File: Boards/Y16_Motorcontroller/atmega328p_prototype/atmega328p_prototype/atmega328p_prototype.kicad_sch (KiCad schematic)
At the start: 14 parts, among them J1 Conn_02x03_Odd_Even, U1 ATMEGA328P-AU, U2 CH340G, Y1 Crystal

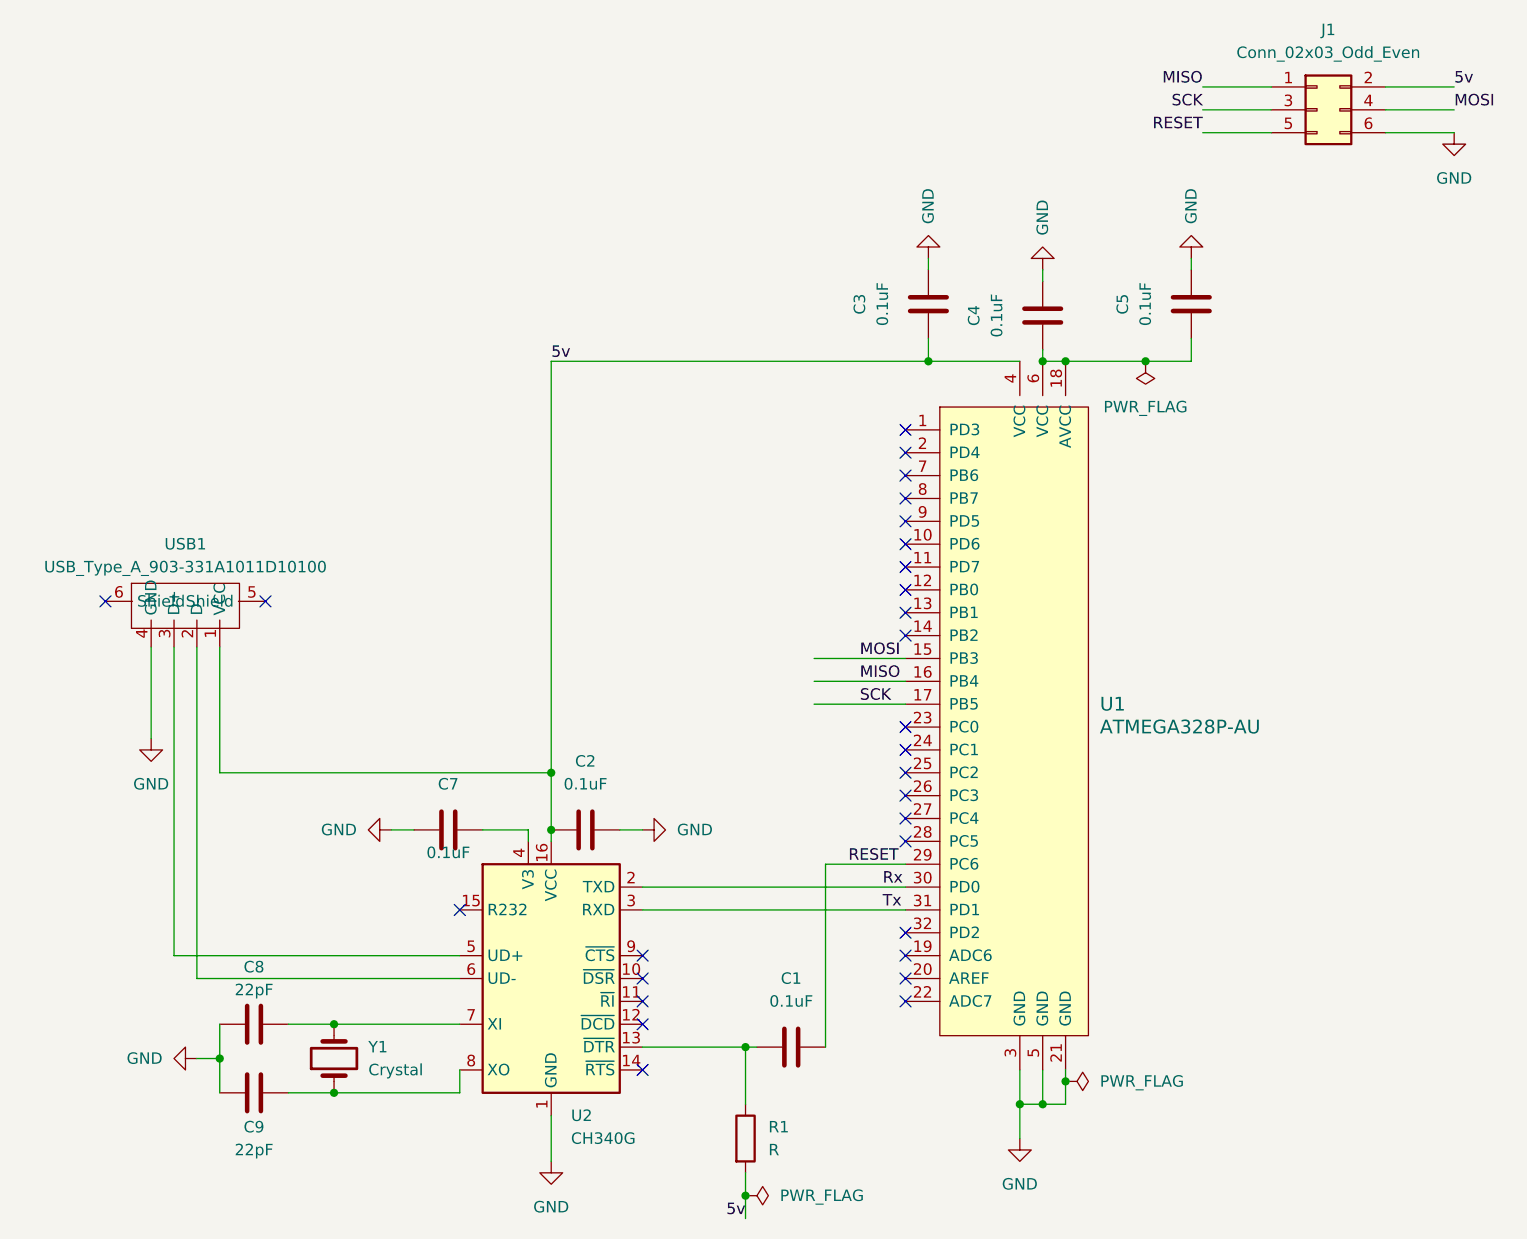
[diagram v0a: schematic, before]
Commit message: added Y16_motorControllerConversion project files
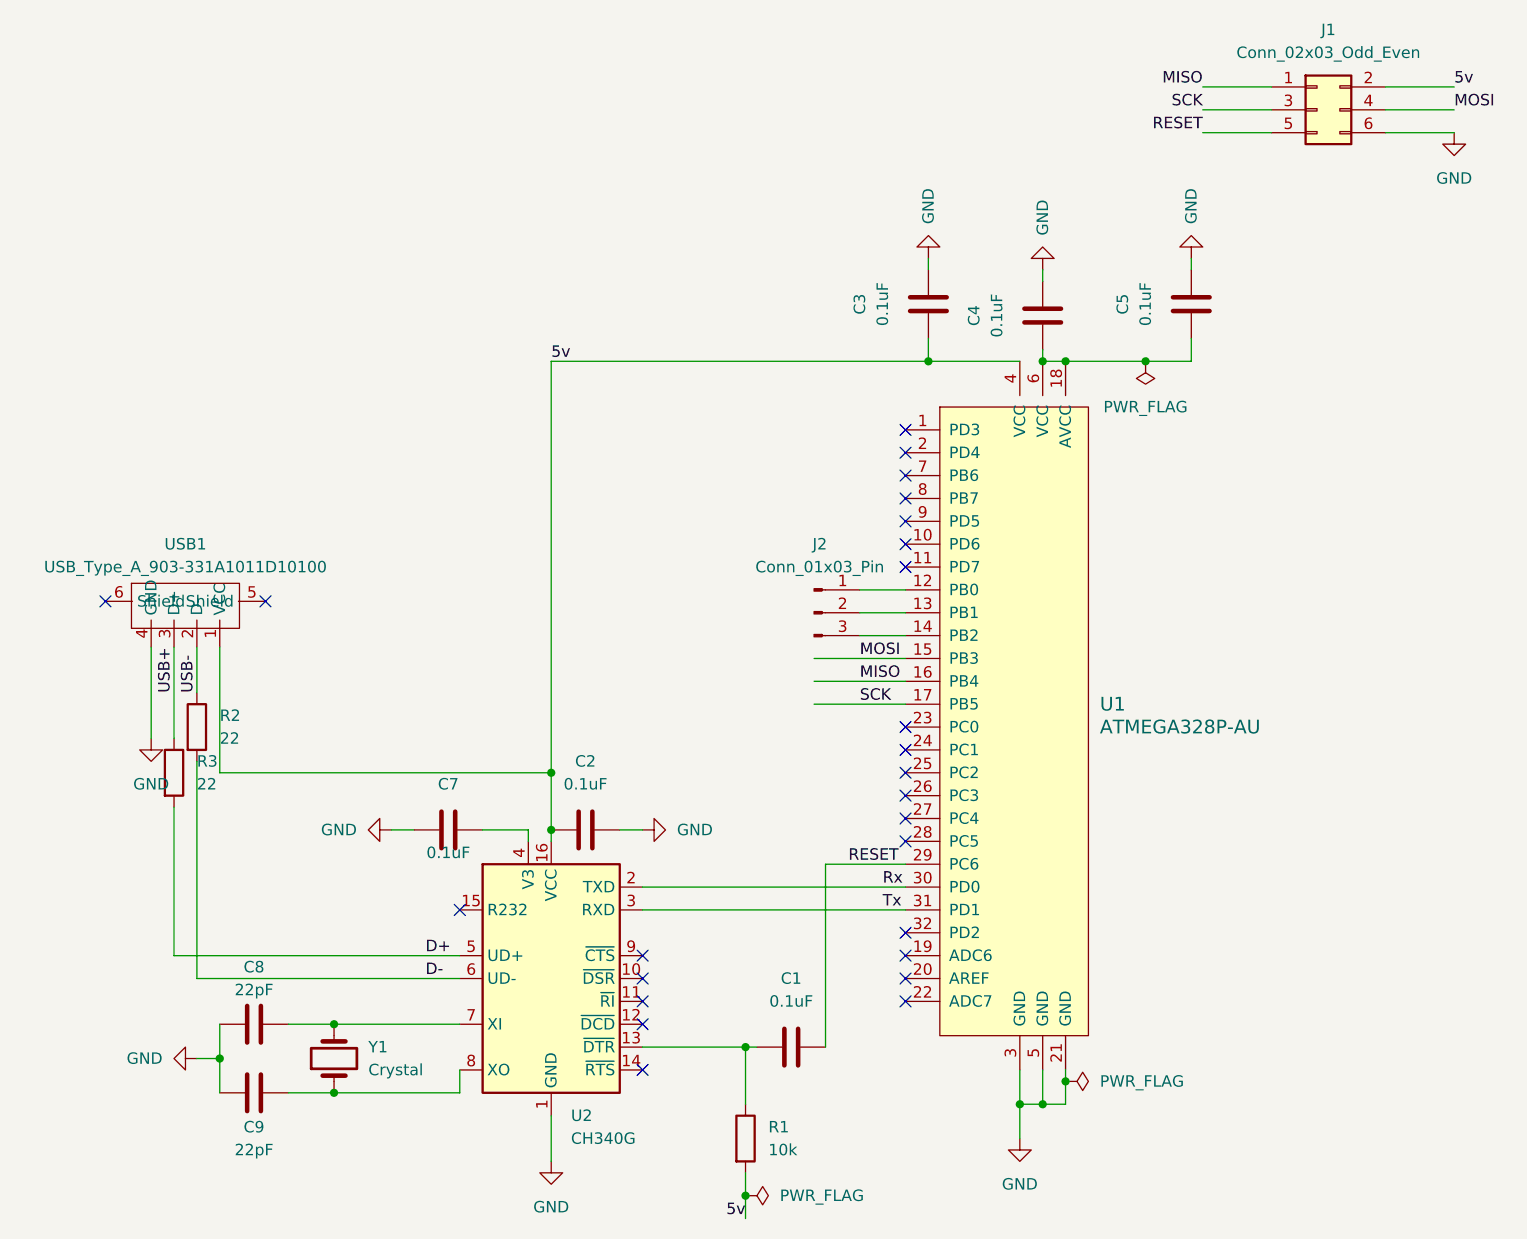
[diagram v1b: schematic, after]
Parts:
- added J2: Conn_01x03_Pin, Connector_PinHeader_2.54mm:PinHeader_1x03_P2.54mm_Vertical, symbol Connector:Conn_01x03_Pin
- added R2, R3: 22, Resistor_SMD:R_0603_1608Metric, symbol Device:R
- C1, C2, C3, C4, C5, C7, C8, C9: footprint (none) -> Capacitor_SMD:C_0603_1608Metric
- J1: footprint (none) -> Connector_PinHeader_2.54mm:PinHeader_2x03_P2.54mm_Vertical
- R1: value R -> 10k; footprint (none) -> Resistor_SMD:R_0603_1608Metric
- USB1: footprint (none) -> PiE_Footprints:USB-A_female
- Y1: footprint (none) -> PiE_Footprints:JYJE S1C12000VWFAC
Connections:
- net at U1.12 (PB0): now also J2.1 (Pin_1)
- net at U1.13 (PB1): now also J2.2 (Pin_2)
- net at U1.14 (PB2): now also J2.3 (Pin_3)
- net D+: now reaches U2.5 (UD+)
- net D+: now also R3.2; no longer USB1.3 (D+)
- net D-: now reaches U2.6 (UD-)
- net D-: now also R2.2; no longer USB1.2 (D-)
- new net USB+: R3.1, USB1.3 (D+)
- new net USB-: R2.1, USB1.2 (D-)
- no-connect marks 28 -> 25
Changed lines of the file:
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@@
   (no_connect (at 116.84 114.3))
   (no_connect (at 166.37 121.92))
-  (no_connect (at 166.37 66.04))
   (no_connect (at 166.37 106.68))
   (no_connect (at 166.37 76.2))
   (no_connect (at 166.37 96.52))
-  (no_connect (at 166.37 63.5))
   (no_connect (at 137.16 127))
   (no_connect (at 137.16 121.92))
-  (no_connect (at 166.37 83.82))
   (no_connect (at 137.16 119.38))
+  (no_connect (at 166.37 60.96))
   (no_connect (at 166.37 93.98))
   (no_connect (at 166.37 101.6))
@@
   (no_connect (at 166.37 104.14))
   (no_connect (at 166.37 99.06))
-  (no_connect (at 166.37 81.28))
   (no_connect (at 166.37 119.38))
   (no_connect (at 95.25 80.01))
   (no_connect (at 137.16 132.08))
-  (no_connect (at 166.37 60.96))
   (no_connect (at 166.37 116.84))
   (no_connect (at 77.47 80.01))
   (no_connect (at 166.37 73.66))
+  (no_connect (at 166.37 63.5))
+  (no_connect (at 166.37 66.04))
   (no_connect (at 166.37 124.46))
   (no_connect (at 137.16 124.46))
-  (no_connect (at 166.37 78.74))
   (wire (pts (xy 148.59 143.51) (xy 148.59 146.05))
     (stroke (width 0) (type default))
@@
     (stroke (width 0) (type default))
   )
+  (wire (pts (xy 161.29 83.82) (xy 166.37 83.82))
+    (stroke (width 0) (type default))
+  )
   (wire (pts (xy 219.71 22.86) (xy 227.33 22.86))
     (stroke (width 0) (type default))
@@
     (stroke (width 0) (type default))
   )
+  (wire (pts (xy 87.63 97.79) (xy 87.63 121.92))
+    (stroke (width 0) (type default))
+  )
   (wire (pts (xy 168.91 43.18) (xy 168.91 41.91))
     (stroke (width 0) (type default))
   )
-  (wire (pts (xy 87.63 85.09) (xy 87.63 121.92))
-    (stroke (width 0) (type default))
-  )
   (wire (pts (xy 157.48 129.54) (xy 157.48 109.22))
     (stroke (width 0) (type default))
@@
     (stroke (width 0) (type default))
   )
+  (wire (pts (xy 161.29 81.28) (xy 166.37 81.28))
+    (stroke (width 0) (type default))
+  )
+  (wire (pts (xy 87.63 85.09) (xy 87.63 90.17))
+    (stroke (width 0) (type default))
+  )
+  (wire (pts (xy 85.09 102.87) (xy 85.09 119.38))
+    (stroke (width 0) (type default))
+  )
   (wire (pts (xy 181.61 53.34) (xy 184.15 53.34))
     (stroke (width 0) (type default))
@@
     (stroke (width 0) (type default))
   )
+  (wire (pts (xy 161.29 78.74) (xy 166.37 78.74))
+    (stroke (width 0) (type default))
+  )
   (wire (pts (xy 90.17 127) (xy 90.17 130.81))
     (stroke (width 0) (type default))
@@
     (stroke (width 0) (type default))
   )
-  (wire (pts (xy 85.09 85.09) (xy 85.09 119.38))
+  (wire (pts (xy 85.09 85.09) (xy 85.09 95.25))
     (stroke (width 0) (type default))
   )
@@
     (effects (font (size 1.27 1.27)) (justify right bottom))
   )
+  (label "D-" (at 113.03 121.92 0) (fields_autoplaced)
+    (effects (font (size 1.27 1.27)) (justify left bottom))
+  )
   (label "MISO" (at 161.29 88.9 0) (fields_autoplaced)
+    (effects (font (size 1.27 1.27)) (justify left bottom))
+  )
+  (label "USB+" (at 85.09 90.17 90) (fields_autoplaced)
     (effects (font (size 1.27 1.27)) (justify left bottom))
   )
@@
     (effects (font (size 1.27 1.27)) (justify right bottom))
   )
+  (label "D+" (at 113.03 119.38 0) (fields_autoplaced)
+    (effects (font (size 1.27 1.27)) (justify left bottom))
+  )
   (label "MOSI" (at 227.33 25.4 0) (fields_autoplaced)
     (effects (font (size 1.27 1.27)) (justify left bottom))
@@
     (effects (font (size 1.27 1.27)) (justify right bottom))
   )
+  (label "USB-" (at 87.63 90.17 90) (fields_autoplaced)
+    (effects (font (size 1.27 1.27)) (justify left bottom))
+  )
   (label "5v" (at 227.33 22.86 0) (fields_autoplaced)
     (effects (font (size 1.27 1.27)) (justify left bottom))
@@
       (effects (font (size 1.27 1.27)))
     )
-    (property "Footprint" "" (at 167.9448 43.18 0)
+    (property "Footprint" "Capacitor_SMD:C_0603_1608Metric" (at 167.9448 43.18 0)
       (effects (font (size 1.27 1.27)) hide)
     )
@@
       (effects (font (size 1.27 1.27)))
     )
-    (property "Footprint" "" (at 180.6448 44.45 0)
+    (property "Footprint" "Capacitor_SMD:C_0603_1608Metric" (at 180.6448 44.45 0)
       (effects (font (size 1.27 1.27)) hide)
     )
@@
       (effects (font (size 1.27 1.27)))
     )
-    (property "Footprint" "" (at 111.76 106.3752 0)
+    (property "Footprint" "Capacitor_SMD:C_0603_1608Metric" (at 111.76 106.3752 0)
       (effects (font (size 1.27 1.27)) hide)
     )
@@
       (effects (font (size 1.27 1.27)))
     )
-    (property "Footprint" "" (at 197.1548 43.18 0)
+    (property "Footprint" "Capacitor_SMD:C_0603_1608Metric" (at 197.1548 43.18 0)
       (effects (font (size 1.27 1.27)) hide)
     )
@@
         (path "/c87bf4b6-f487-4f51-aaac-6d9ce8b1ee73"
           (reference "C5") (unit 1)
+        )
+      )
+    )
+  )
+  (symbol (lib_id "Device:R") (at 85.09 99.06 0) (unit 1)
+    (in_bom yes) (on_board yes) (dnp no) (fields_autoplaced)
+    (property "Reference" "R3" (at 87.63 97.79 0)
+      (effects (font (size 1.27 1.27)) (justify left))
+    )
+    (property "Value" "22" (at 87.63 100.33 0)
+      (effects (font (size 1.27 1.27)) (justify left))
+    )
+    (property "Footprint" "Resistor_SMD:R_0603_1608Metric" (at 83.312 99.06 90)
+      (effects (font (size 1.27 1.27)) hide)
+    )
+    (property "Datasheet" "~" (at 85.09 99.06 0)
+      (effects (font (size 1.27 1.27)) hide)
+    )
+    (pin "1")
+    (pin "2")
+    (instances
+      (project "atmega328p_prototype"
+        (path "/c87bf4b6-f487-4f51-aaac-6d9ce8b1ee73"
+          (reference "R3") (unit 1)
         )
       )
@@
       (effects (font (size 1.27 1.27)))
     )
-    (property "Footprint" "" (at 90.17 135.5852 0)
+    (property "Footprint" "Capacitor_SMD:C_0603_1608Metric" (at 90.17 135.5852 0)
       (effects (font (size 1.27 1.27)) hide)
     )
@@
       (effects (font (size 1.27 1.27)) (justify right))
     )
-    (property "Footprint" "" (at 102.87 130.81 0)
+    (property "Footprint" "PiE_Footprints:JYJE S1C12000VWFAC" (at 102.87 130.81 0)
       (effects (font (size 1.27 1.27)) hide)
     )
@@
       (effects (font (size 1.27 1.27)))
     )
-    (property "Footprint" "" (at 134.62 104.4448 0)
+    (property "Footprint" "Capacitor_SMD:C_0603_1608Metric" (at 134.62 104.4448 0)
       (effects (font (size 1.27 1.27)) hide)
     )
@@
       (effects (font (size 1.27 1.27)))
     )
-    (property "Footprint" "" (at 157.48 128.5748 0)
+    (property "Footprint" "Capacitor_SMD:C_0603_1608Metric" (at 157.48 128.5748 0)
       (effects (font (size 1.27 1.27)) hide)
     )
@@
         (path "/c87bf4b6-f487-4f51-aaac-6d9ce8b1ee73"
           (reference "#PWR01") (unit 1)
+        )
+      )
+    )
+  )
+  (symbol (lib_id "Connector:Conn_01x03_Pin") (at 156.21 81.28 0) (unit 1)
+    (in_bom yes) (on_board yes) (dnp no) (fields_autoplaced)
+    (property "Reference" "J2" (at 156.845 73.66 0)
+      (effects (font (size 1.27 1.27)))
+    )
+    (property "Value" "Conn_01x03_Pin" (at 156.845 76.2 0)
+      (effects (font (size 1.27 1.27)))
+    )
+    (property "Footprint" "Connector_PinHeader_2.54mm:PinHeader_1x03_P2.54mm_Vertical" (at 156.21 81.28 0)
+      (effects (font (size 1.27 1.27)) hide)
+    )
+    (property "Datasheet" "~" (at 156.21 81.28 0)
+      (effects (font (size 1.27 1.27)) hide)
+    )
+    (pin "1")
+    (pin "2")
+    (pin "3")
+    (instances
+      (project "atmega328p_prototype"
+        (path "/c87bf4b6-f487-4f51-aaac-6d9ce8b1ee73"
+          (reference "J2") (unit 1)
         )
       )
@@
       (effects (font (size 1.27 1.27)))
     )
-    (property "Footprint" "" (at 97.79 126.0348 0)
+    (property "Footprint" "Capacitor_SMD:C_0603_1608Metric" (at 97.79 126.0348 0)
       (effects (font (size 1.27 1.27)) hide)
     )
@@
       (effects (font (size 1.27 1.27)) (justify left))
     )
-    (property "Value" "R" (at 151.13 140.97 0)
+    (property "Value" "10k" (at 151.13 140.97 0)
       (effects (font (size 1.27 1.27)) (justify left))
     )
-    (property "Footprint" "" (at 146.812 139.7 90)
+    (property "Footprint" "Resistor_SMD:R_0603_1608Metric" (at 146.812 139.7 90)
       (effects (font (size 1.27 1.27)) hide)
     )
@@
     )
   )
+  (symbol (lib_id "Device:R") (at 87.63 93.98 0) (unit 1)
+    (in_bom yes) (on_board yes) (dnp no) (fields_autoplaced)
+    (property "Reference" "R2" (at 90.17 92.71 0)
+      (effects (font (size 1.27 1.27)) (justify left))
+    )
+    (property "Value" "22" (at 90.17 95.25 0)
+      (effects (font (size 1.27 1.27)) (justify left))
+    )
+    (property "Footprint" "Resistor_SMD:R_0603_1608Metric" (at 85.852 93.98 90)
+      (effects (font (size 1.27 1.27)) hide)
+    )
+    (property "Datasheet" "~" (at 87.63 93.98 0)
+      (effects (font (size 1.27 1.27)) hide)
+    )
+    (pin "1")
+    (pin "2")
+    (instances
+      (project "atmega328p_prototype"
+        (path "/c87bf4b6-f487-4f51-aaac-6d9ce8b1ee73"
+          (reference "R2") (unit 1)
+        )
+      )
+    )
+  )
   (symbol (lib_id "Connector_Generic:Conn_02x03_Odd_Even") (at 212.09 25.4 0) (unit 1)
     (in_bom yes) (on_board yes) (dnp no) (fields_autoplaced)
@@
       (effects (font (size 1.27 1.27)))
     )
-    (property "Footprint" "" (at 212.09 25.4 0)
+    (property "Footprint" "Connector_PinHeader_2.54mm:PinHeader_2x03_P2.54mm_Vertical" (at 212.09 25.4 0)
       (effects (font (size 1.27 1.27)) hide)
     )
@@
       (effects (font (size 1.27 1.27)))
     )
-    (property "Footprint" "" (at 86.36 80.01 0)
-      (effects (font (size 1.27 1.27)) hide)
-    )
+    (property "Footprint" "PiE_Footprints:USB-A_female" (at 86.36 80.01 0)
+      (effects (font (size 1.27 1.27)) hide)
+    )
